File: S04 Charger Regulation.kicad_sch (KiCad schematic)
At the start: 24 parts, among them Q6 DMT4011LFG, Q7 DMT4011LFG, U1 LTC1960

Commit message: BOM consolidation, OVLO divider to 1%, U5 fixes and I2C config option
- Consolidate passives: 1uF 50V to 0603, 100nF to 50V X7R 0402,
  10uF to 50V X7R 1210, 220nF to 0603, 10R to 0402 (100 -> 90 BOM lines)
- TPS22811 OVLO divider 1M/102K 0.1% -> 1M/100K 1% (12.6V min trip)
- U5 LM51772: C30 -> R102 10K to GND (VCC1 disabled), C32 -> 22uF 16V 0805,
  R29 1.9K -> 1.87K to sit inside the CFG4 window
- Add DNP I2C configuration option for U5 (R103-R107) on J3.34/J3.36,
  shared with R97/R98 fallback
- Document all changes in README.md

Co-Authored-By: Claude Opus 5.5 <noreply@anthropic.com>
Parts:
- C13, C14: footprint Capacitor_SMD:C_1206_3216Metric -> Capacitor_SMD:C_1210_3225Metric; symbol Lattech Systems:Capacitor 10uF 50V X5R 1206 -> Lattech Systems:Capacitor 10uF 50V X7R 1210; ALTIUM_FOOTPRINT 1206 -> 1210; MANUFACTURER_PN CGA5L1X7R1H106K160AC -> GRM32ER71H106KA12L; MATERIAL X5R -> X7R
- C16: footprint Capacitor_SMD:C_0805_2012Metric -> Capacitor_SMD:C_0603_1608Metric; symbol Lattech Systems:Capacitor 220nF 50V X7R 0805 -> Lattech Systems:Capacitor 220nF 50V X7R 0603; ALTIUM_FOOTPRINT 0805 -> 0603; MANUFACTURER_PN CC0805KFX7R9BB224 -> CC0603KRX7R9BB224
- C17, C18, C20, C21: MANUFACTURER ? -> Yageo; MANUFACTURER_PN ? -> CC0402KPX7R9BB104
- C22: MANUFACTURER (none) -> Yageo; MANUFACTURER_PN (none) -> CC0603KRX7R9BB224; MATERIAL X5R -> X7R; PL_SORT_GROUP (none) -> 2.3
- C24, C25, C26: footprint Capacitor_SMD:C_1206_3216Metric -> Capacitor_SMD:C_1210_3225Metric; symbol Lattech Systems:Capacitor 10uF 25V X7R 1206 -> Lattech Systems:Capacitor 10uF 50V X7R 1210; ALTIUM_FOOTPRINT 1206 -> 1210; MANUFACTURER ? -> Murata; MANUFACTURER_PN ? -> GRM32ER71H106KA12L; VOLTAGE 25V -> 50V
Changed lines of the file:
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@@
 	)
 	(symbol
-		(lib_id "Lattech Systems:Capacitor 10uF 25V X7R 1206")
+		(lib_id "Lattech Systems:Capacitor 10uF 50V X7R 1210")
 		(at 297.18 99.06 90)
 		(unit 1)
@@
 			)
 		)
-		(property "Footprint" "Capacitor_SMD:C_1206_3216Metric"
+		(property "Footprint" "Capacitor_SMD:C_1210_3225Metric"
 			(at 297.18 99.06 0)
 			(hide yes)
@@
 			)
 		)
-		(property "Description" "Capacitor 10uF 25V X7R 1206"
+		(property "Description" "Capacitor 10uF 50V X7R 1210"
 			(at 297.18 99.06 0)
 			(hide yes)
@@
 			)
 		)
-		(property "MANUFACTURER" "?"
+		(property "MANUFACTURER" "Murata"
 			(at 295.91 94.742 90)
 			(hide yes)
@@
 			)
 		)
-		(property "MANUFACTURER_PN" "?"
+		(property "MANUFACTURER_PN" "GRM32ER71H106KA12L"
 			(at 295.91 94.742 90)
 			(hide yes)
@@
 			)
 		)
-		(property "ALTIUM_FOOTPRINT" "1206"
+		(property "ALTIUM_FOOTPRINT" "1210"
 			(at 298.45 103.378 90)
 			(show_name no)
@@
 			)
 		)
-		(property "VOLTAGE" "25V"
+		(property "VOLTAGE" "50V"
 			(at 298.45 107.95 90)
 			(show_name no)
@@
 	)
 	(symbol
-		(lib_id "Lattech Systems:Capacitor 10uF 50V X5R 1206")
+		(lib_id "Lattech Systems:Capacitor 10uF 50V X7R 1210")
 		(at 77.47 97.79 90)
 		(unit 1)
@@
 			)
 		)
-		(property "Footprint" "Capacitor_SMD:C_1206_3216Metric"
+		(property "Footprint" "Capacitor_SMD:C_1210_3225Metric"
 			(at 77.47 97.79 0)
 			(hide yes)
@@
 			)
 		)
-		(property "Description" "Capacitor 10uF 50V X5R 1206"
+		(property "Description" "Capacitor 10uF 50V X7R 1210"
 			(at 77.47 97.79 0)
 			(hide yes)
@@
 			)
 		)
-		(property "MANUFACTURER_PN" "CGA5L1X7R1H106K160AC"
+		(property "MANUFACTURER_PN" "GRM32ER71H106KA12L"
 			(at 76.2 93.472 90)
 			(hide yes)
@@
 			)
 		)
-		(property "ALTIUM_FOOTPRINT" "1206"
+		(property "ALTIUM_FOOTPRINT" "1210"
 			(at 78.74 102.108 90)
 			(show_name no)
@@
 			)
 		)
-		(property "MATERIAL" "X5R"
+		(property "MATERIAL" "X7R"
 			(at 78.74 104.14 90)
 			(show_name no)
@@
 			)
 		)
-		(property "MANUFACTURER" "?"
+		(property "MANUFACTURER" "Yageo"
 			(at 246.38 140.462 90)
 			(hide yes)
@@
 			)
 		)
-		(property "MANUFACTURER_PN" "?"
+		(property "MANUFACTURER_PN" "CC0402KPX7R9BB104"
 			(at 246.38 140.462 90)
 			(hide yes)
@@
 	)
 	(symbol
-		(lib_id "Lattech Systems:Capacitor 10uF 25V X7R 1206")
+		(lib_id "Lattech Systems:Capacitor 10uF 50V X7R 1210")
 		(at 284.48 99.06 90)
 		(unit 1)
@@
 			)
 		)
-		(property "Footprint" "Capacitor_SMD:C_1206_3216Metric"
+		(property "Footprint" "Capacitor_SMD:C_1210_3225Metric"
 			(at 284.48 99.06 0)
 			(hide yes)
@@
 			)
 		)
-		(property "Description" "Capacitor 10uF 25V X7R 1206"
+		(property "Description" "Capacitor 10uF 50V X7R 1210"
 			(at 284.48 99.06 0)
 			(hide yes)
@@
 			)
 		)
-		(property "MANUFACTURER" "?"
+		(property "MANUFACTURER" "Murata"
 			(at 283.21 94.742 90)
 			(hide yes)
@@
 			)
 		)
-		(property "MANUFACTURER_PN" "?"
+		(property "MANUFACTURER_PN" "GRM32ER71H106KA12L"
 			(at 283.21 94.742 90)
 			(hide yes)
@@
 			)
 		)
-		(property "ALTIUM_FOOTPRINT" "1206"
+		(property "ALTIUM_FOOTPRINT" "1210"
 			(at 285.75 103.378 90)
 			(show_name no)
@@
 			)
 		)
-		(property "VOLTAGE" "25V"
+		(property "VOLTAGE" "50V"
 			(at 285.75 107.95 90)
 			(show_name no)
@@
 	)
 	(symbol
-		(lib_id "Lattech Systems:Capacitor 10uF 25V X7R 1206")
+		(lib_id "Lattech Systems:Capacitor 10uF 50V X7R 1210")
 		(at 309.88 99.06 90)
 		(unit 1)
@@
 			)
 		)
-		(property "Footprint" "Capacitor_SMD:C_1206_3216Metric"
+		(property "Footprint" "Capacitor_SMD:C_1210_3225Metric"
 			(at 309.88 99.06 0)
 			(hide yes)
@@
 			)
 		)
-		(property "Description" "Capacitor 10uF 25V X7R 1206"
+		(property "Description" "Capacitor 10uF 50V X7R 1210"
 			(at 309.88 99.06 0)
 			(hide yes)
@@
 			)
 		)
-		(property "MANUFACTURER" "?"
+		(property "MANUFACTURER" "Murata"
 			(at 308.61 94.742 90)
 			(hide yes)
@@
 			)
 		)
-		(property "MANUFACTURER_PN" "?"
+		(property "MANUFACTURER_PN" "GRM32ER71H106KA12L"
 			(at 308.61 94.742 90)
 			(hide yes)
@@
 			)
 		)
-		(property "ALTIUM_FOOTPRINT" "1206"
+		(property "ALTIUM_FOOTPRINT" "1210"
 			(at 311.15 103.378 90)
 			(show_name no)
@@
 			)
 		)
-		(property "VOLTAGE" "25V"
+		(property "VOLTAGE" "50V"
 			(at 311.15 107.95 90)
 			(show_name no)
@@
 			)
 		)
-		(property "PL_SORT_GROUP" ""
+		(property "PL_SORT_GROUP" "2.3"
 			(at 246.38 176.022 90)
 			(hide yes)
@@
 			)
 		)
-		(property "MANUFACTURER" ""
+		(property "MANUFACTURER" "Yageo"
 			(at 246.38 176.022 90)
 			(hide yes)
@@
 			)
 		)
-		(property "MANUFACTURER_PN" ""
+		(property "MANUFACTURER_PN" "CC0603KRX7R9BB224"
 			(at 246.38 176.022 90)
 			(hide yes)
@@
 			)
 		)
-		(property "MATERIAL" "X5R"
+		(property "MATERIAL" "X7R"
 			(at 248.92 186.69 90)
 			(show_name no)
@@
 			)
 		)
-		(property "MANUFACTURER" "?"
+		(property "MANUFACTURER" "Yageo"
 			(at 158.75 168.402 90)
 			(hide yes)
@@
 			)
 		)
-		(property "MANUFACTURER_PN" "?"
+		(property "MANUFACTURER_PN" "CC0402KPX7R9BB104"
 			(at 158.75 168.402 90)
 			(hide yes)
@@
 	)
 	(symbol
-		(lib_id "Lattech Systems:Capacitor 220nF 50V X7R 0805")
+		(lib_id "Lattech Systems:Capacitor 220nF 50V X7R 0603")
 		(at 160.02 97.79 90)
 		(unit 1)
@@
 			)
 		)
-		(property "Footprint" "Capacitor_SMD:C_0805_2012Metric"
+		(property "Footprint" "Capacitor_SMD:C_0603_1608Metric"
 			(at 160.02 97.79 0)
 			(hide yes)
@@
 			)
 		)
-		(property "Description" "Capacitor 220nF 50V X7R 0805"
+		(property "Description" "Capacitor 220nF 50V X7R 0603"
 			(at 160.02 97.79 0)
 			(hide yes)
@@
 			)
 		)
-		(property "MANUFACTURER_PN" "CC0805KFX7R9BB224"
+		(property "MANUFACTURER_PN" "CC0603KRX7R9BB224"
 			(at 158.75 93.472 90)
 			(hide yes)
@@
 			)
 		)
-		(property "ALTIUM_FOOTPRINT" "0805"
+		(property "ALTIUM_FOOTPRINT" "0603"
 			(at 161.29 102.108 90)
 			(show_name no)
@@
 	)
 	(symbol
-		(lib_id "Lattech Systems:Capacitor 10uF 50V X5R 1206")
+		(lib_id "Lattech Systems:Capacitor 10uF 50V X7R 1210")
 		(at 88.9 97.79 90)
 		(unit 1)
@@
 			)
 		)
-		(property "Footprint" "Capacitor_SMD:C_1206_3216Metric"
+		(property "Footprint" "Capacitor_SMD:C_1210_3225Metric"
 			(at 88.9 97.79 0)
 			(hide yes)
@@
 			)
 		)
-		(property "Description" "Capacitor 10uF 50V X5R 1206"
+		(property "Description" "Capacitor 10uF 50V X7R 1210"
 			(at 88.9 97.79 0)
 			(hide yes)
@@
 			)
 		)
-		(property "MANUFACTURER_PN" "CGA5L1X7R1H106K160AC"
+		(property "MANUFACTURER_PN" "GRM32ER71H106KA12L"
 			(at 87.63 93.472 90)
 			(hide yes)
@@
 			)
 		)
-		(property "ALTIUM_FOOTPRINT" "1206"
+		(property "ALTIUM_FOOTPRINT" "1210"
 			(at 90.17 102.108 90)
 			(show_name no)
@@
 			)
 		)
-		(property "MATERIAL" "X5R"
+		(property "MATERIAL" "X7R"
 			(at 90.17 104.14 90)
 			(show_name no)
@@
 			)
 		)
-		(property "MANUFACTURER" "?"
+		(property "MANUFACTURER" "Yageo"
 			(at 231.14 176.022 90)
 			(hide yes)
@@
 			)
 		)
-		(property "MANUFACTURER_PN" "?"
+		(property "MANUFACTURER_PN" "CC0402KPX7R9BB104"
 			(at 231.14 176.022 90)
 			(hide yes)
@@
 			)
 		)
-		(property "MANUFACTURER" "?"
+		(property "MANUFACTURER" "Yageo"
 			(at 210.82 176.022 90)
 			(hide yes)
@@
 			)
 		)
-		(property "MANUFACTURER_PN" "?"
+		(property "MANUFACTURER_PN" "CC0402KPX7R9BB104"
 			(at 210.82 176.022 90)
 			(hide yes)

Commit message: Final-revision value changes and standard R/C symbols
Values (schematic and PCB):
- C2 100uF -> 82uF, matching the ordered 35SVPF82M
- C46, C47, C51 (TPS22811 DVDT) 4.7nF -> 1.8nF CC0402KRX7R9BB182 for a
  shorter output ramp
- R24-R27 10R -> 0R; D9, D10 and R36 DNP
- R14 0.01R -> 0.012R PA2512FKF7W0R012E

Symbols:
- All 160 resistors and capacitors now use Device:R, Device:C and
  Device:C_Polarized; the 76 per-value R/C symbols are removed from the
  project library. Connectivity is unchanged (netlist compared).
- Value is now the displayed field instead of ALTIUM_VALUE, which had left
  R1, C39 and R54 showing their old values. ALTIUM_VALUE synced with Value
  on R1, C39, R54, D1, Q1, Q3 and L1.
- Net-(C40-+) is now Net-(U5-ISNSP); renamed on the PCB and in the
  PWR 15A net class pattern.

Co-Authored-By: Claude Opus 5.5 <noreply@anthropic.com>
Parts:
- C13, C14, C24, C25, C26: symbol Lattech Systems:Capacitor 10uF 50V X7R 1210 -> Device:C
- C15: symbol Lattech Systems:Capacitor 4.7uF 10V X5R 0805 -> Device:C
- C16, C22: symbol Lattech Systems:Capacitor 220nF 50V X7R 0603 -> Device:C
- C17, C18, C20, C21: symbol Lattech Systems:Capacitor 100nF 50V X7R 0402 -> Device:C
- C19: symbol Lattech Systems:Capacitor 100pF 50V C0G 0402 -> Device:C
- C23: symbol Lattech Systems:Capacitor 1uF 50V X5R 0603 -> Device:C
- L1: ALTIUM_VALUE 4.7uH -> 10uH
- R19: symbol Lattech Systems:Resistor 0.015R 1% 3W 2512 -> Device:R
- R20: symbol Lattech Systems:Resistor 3.6K 1% 0402 -> Device:R
- R21: symbol Lattech Systems:Resistor 100R 1% 0402 -> Device:R

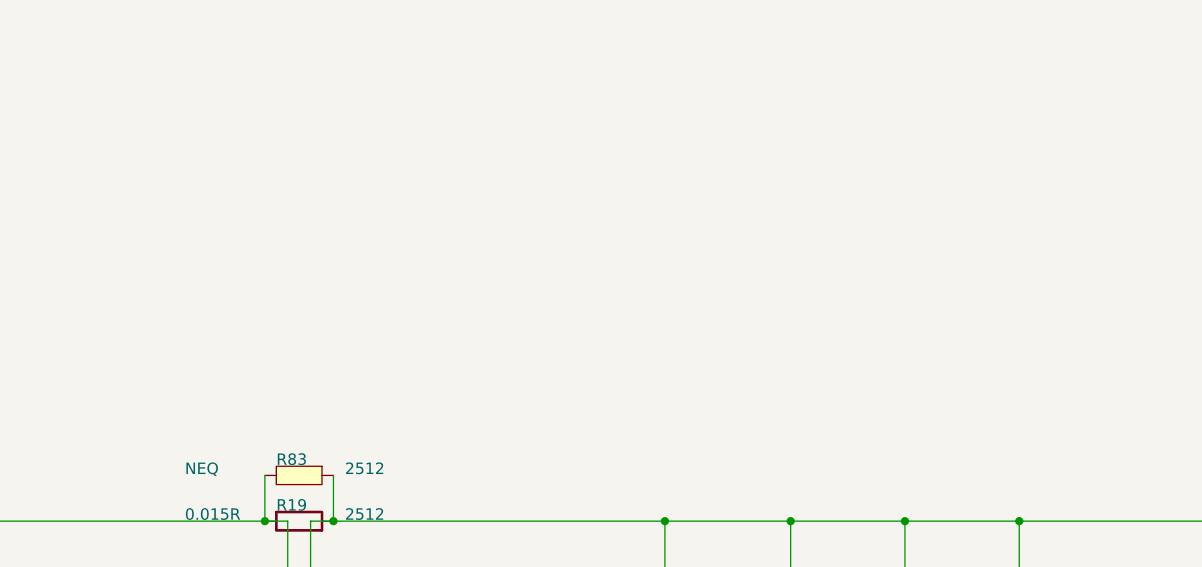
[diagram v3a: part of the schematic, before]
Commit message: Retune load-switch OVLO and PG dividers; add design constraint notes
- R90-R92 1M -> 1.07M: OVLO trips at 14.0 V (13.40-14.69 V) and recovers
  below 12.75 V (at least 12.23 V), so a tripped switch always comes back
  on the 12.03 V rail. R101 (Q23 gate divider) -> 1.07M to share the line.
- PGTH dividers R59/R61/R76 1M -> 100K and R60/R62/R77 130K -> 13K: same
  10.43 V threshold, but the +-1 uA pin leakage now moves it 0.1 V, not
  1 V; worst-case rising 10.93 V instead of 11.84 V.
- Schematic notes for the W16 constraints: J2 contacts (S01), R16 latching
  breaker and ED29/QE29 trip currents (S03), R19 vs L1 saturation (S04),
  R22 presence pull-up (S05), R42 and the U5 MODE/ILIMCOMP/VCC2 pins (S06),
  and the OVLO/PG divider settings (S07).
- README: OVLO and PG divider figures, and the EN_CONST_TDEAD default for
  the I2C build.

Co-Authored-By: Claude Opus 5.5 <noreply@anthropic.com>
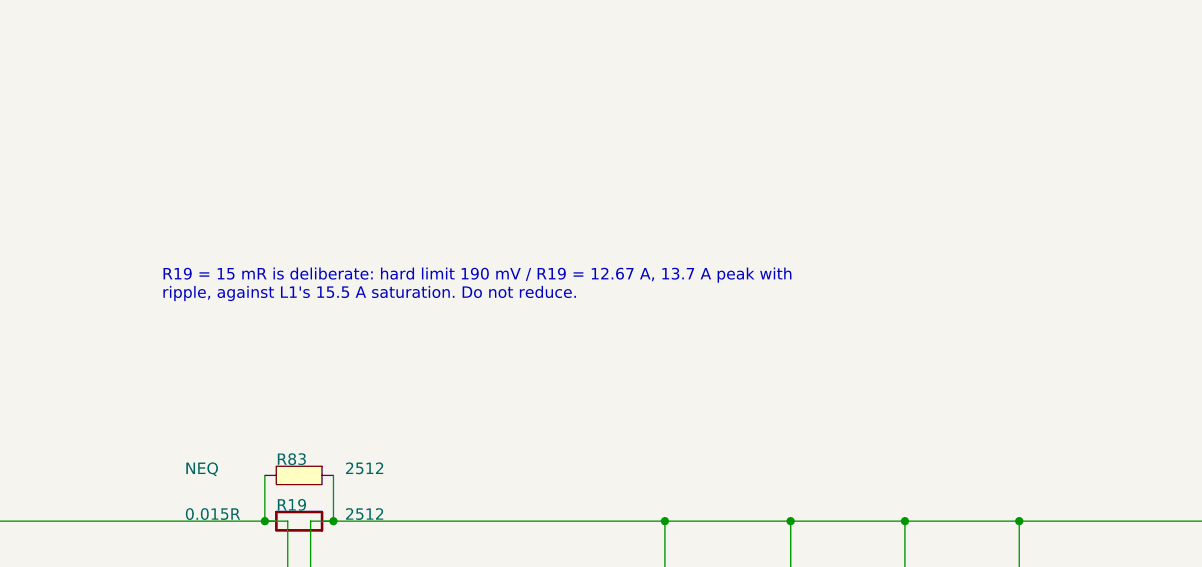
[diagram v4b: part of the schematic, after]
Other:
- note added: "R19 = 15 mR is deliberate: hard limit 190 mV / R19 = 12.67 A, 13.7 A peak with ripple, against L1's 15.5 A saturation. Do not reduce."
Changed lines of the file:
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@@
+		)
+	)
+	(text "R19 = 15 mR is deliberate: hard limit 190 mV / R19 = 12.67 A, 13.7 A peak with\nripple, against L1's 15.5 A saturation. Do not reduce."
+		(exclude_from_sim no)
+		(at 214.63 59.69 0)
+		(effects
+			(font
+				(size 1.27 1.27)
+			)
+			(justify left top)
 		)
 	)

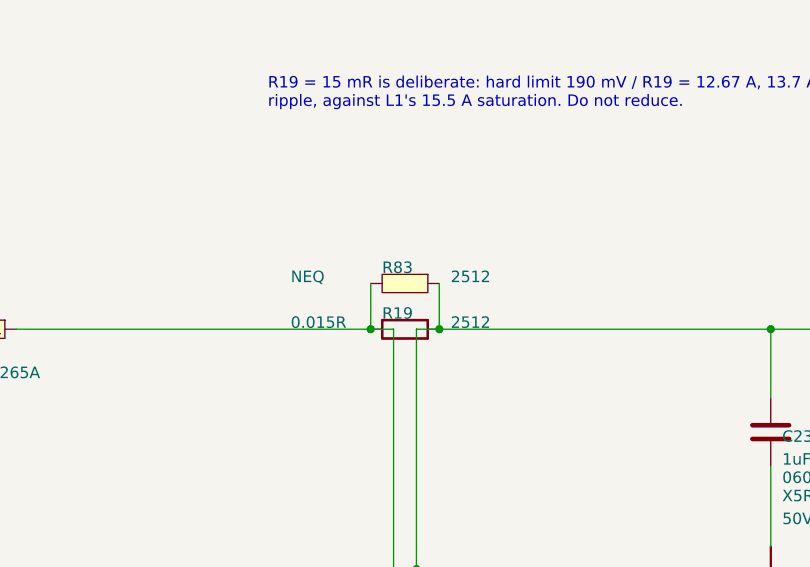
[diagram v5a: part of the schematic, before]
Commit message: U11 PCAL9714HNMP 3D model; FET zone reshaping; R23/R82-R85 DNP
- U11 moves to a project-library copy of HVQFN-24-1EP_4x4mm_P0.5mm_EP2.6x2.6mm
  linked to ${KIPRJMOD}/PCAL9714HNMP.stp (STEP later embedded; file not kept). Schematic and Lattech
  symbol point at the project copy.
- Board updated from the schematic (symbol pin data on the swapped
  footprints) and zone fills reshaped around the FETs.
- R23, R82-R85 (NEQ) set DNP in the schematic and on the board.

DRC: 0 errors, 0 unconnected, 0 schematic parity issues. ERC: 0 violations.

Co-Authored-By: Claude Opus 5.5 <noreply@anthropic.com>
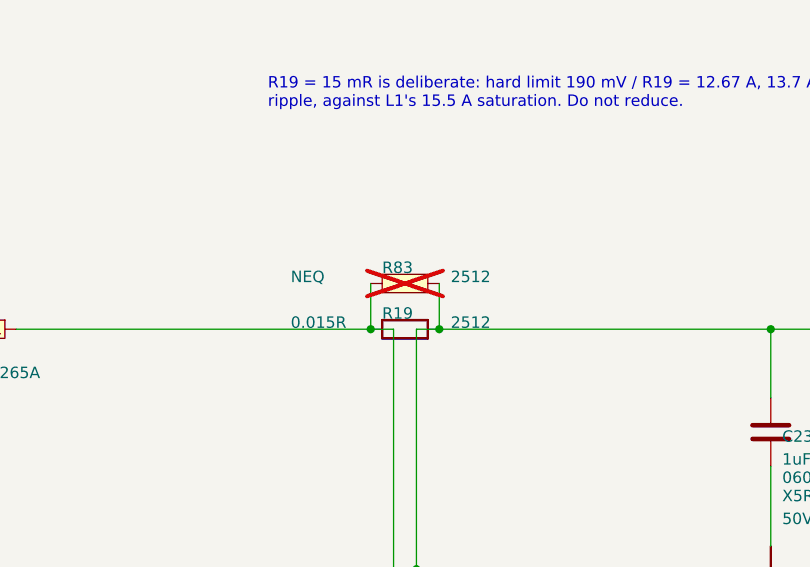
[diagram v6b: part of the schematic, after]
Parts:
- R83: now not fitted
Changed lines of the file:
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@@
 		(on_board yes)
 		(in_pos_files yes)
-		(dnp no)
+		(dnp yes)
 		(property "Reference" "R83"
 			(at 227.33 81.534 0)
